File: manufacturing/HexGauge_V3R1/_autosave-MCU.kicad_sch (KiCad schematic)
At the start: 26 parts, among them SW2 SW_Omron_B3FS, SW2 SW_SPDT, U2 STM32F405RGT6, Y1 25MHz 12pF

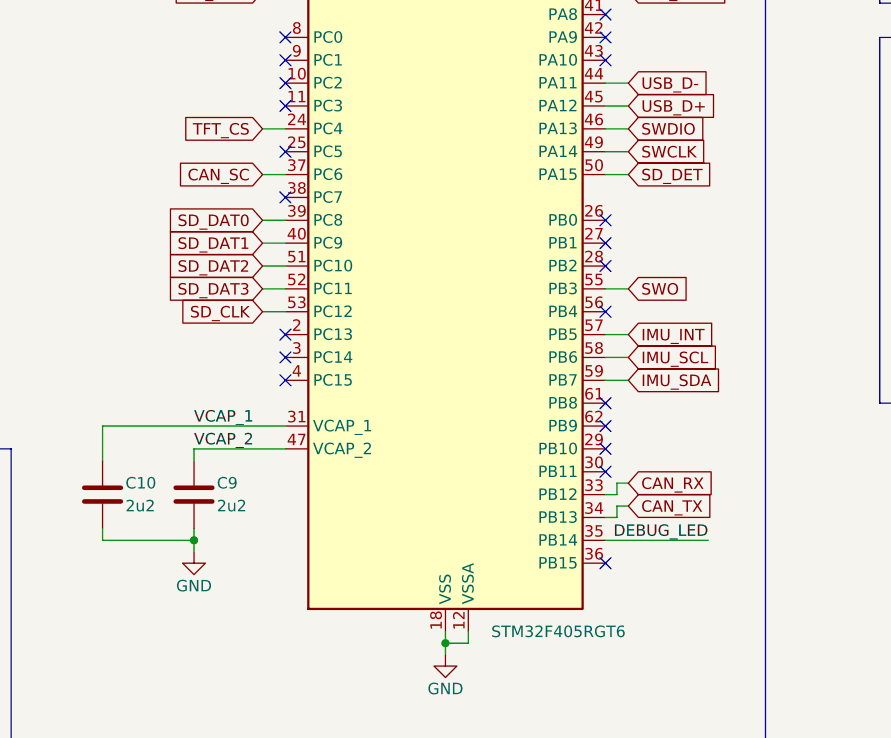
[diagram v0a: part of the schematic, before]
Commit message: Cleaned Up Schematic
Added Blockdiagram
Reannotated Symbols
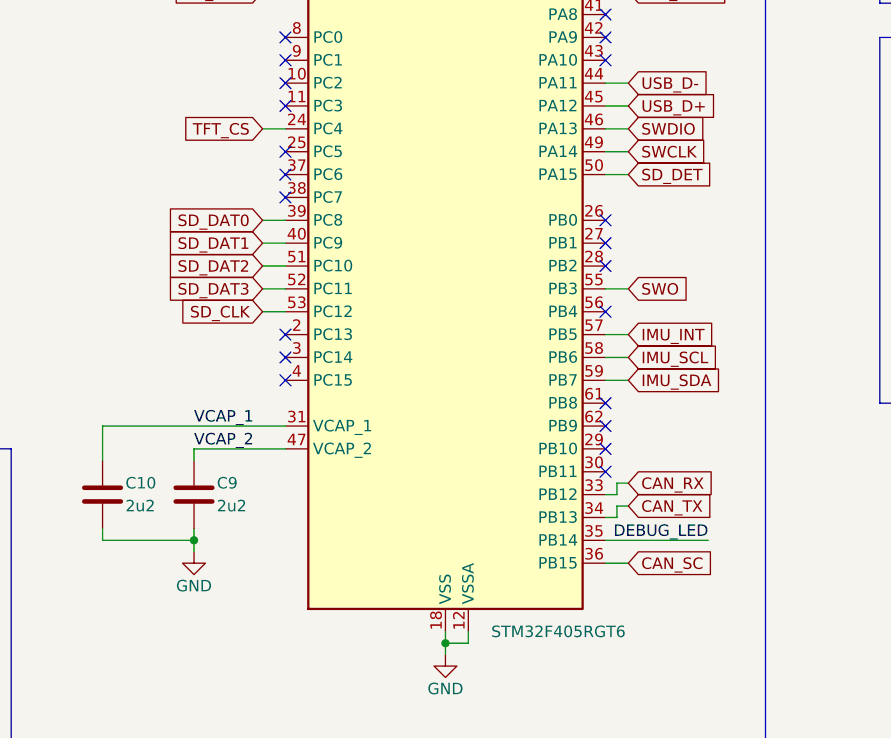
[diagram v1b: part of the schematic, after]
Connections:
- net CAN_SC: now also U2.36 (PB15); no longer U2.37 (PC6)
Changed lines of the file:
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@@
   (no_connect (at 121.92 113.03))
   (no_connect (at 86.36 95.25))
+  (no_connect (at 86.36 107.95))
   (no_connect (at 86.36 100.33))
   (no_connect (at 121.92 115.57))
@@
   (no_connect (at 121.92 90.17))
   (no_connect (at 121.92 133.35))
-  (no_connect (at 121.92 151.13))
   (no_connect (at 86.36 105.41))
   (wire (pts (xy 124.46 80.01) (xy 121.92 80.01))
@@
     (stroke (width 0) (type default))
   )
+  (wire (pts (xy 124.46 151.13) (xy 121.92 151.13))
+    (stroke (width 0) (type default))
+  )
   (wire (pts (xy 45.72 58.42) (xy 45.72 59.69))
     (stroke (width 0) (type default))
@@
   )
   (wire (pts (xy 45.72 59.69) (xy 34.29 59.69))
-    (stroke (width 0) (type default))
-  )
-  (wire (pts (xy 83.82 107.95) (xy 86.36 107.95))
     (stroke (width 0) (type default))
   )
@@
     )
   )
+  (global_label "CAN_SC" (shape input) (at 124.46 151.13 0) (fields_autoplaced)
+    (effects (font (size 1.27 1.27)) (justify left))
+    (property "Intersheetrefs" "${INTERSHEET_REFS}" (at 134.502 151.13 0)
+      (effects (font (size 1.27 1.27)) (justify left) hide)
+    )
+  )
   (global_label "TFT_MOSI" (shape input) (at 124.46 87.63 0) (fields_autoplaced)
     (effects (font (size 1.27 1.27)) (justify left))
@@
       (effects (font (size 1.27 1.27)) (justify right) hide)
     )
-  )
-  (global_label "CAN_SC" (shape input) (at 83.82 107.95 180) (fields_autoplaced)
-    (effects (font (size 1.27 1.27)) (justify right))
-    (property "Intersheetrefs" "${INTERSHEET_REFS}" (at 73.778 107.95 0)
-      (effects (font (size 1.27 1.27)) (justify right) hide)
-    )
